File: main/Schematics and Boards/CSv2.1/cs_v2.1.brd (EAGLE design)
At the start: 38.1 x 47 mm, 78 parts, among them J101 J-JTAG-CORTEX-NEEDLE6-LEGS, J301 HIROSE-DF40_50-PIN_CONNECTORS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, J302 HIROSE-DF40_50-PIN_CONNECTORS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, Q1 DMG3415UFY4Q-7F, U1 NCP708MU330TAG, U101 ATSAMD51, U2 W25N01GVZEIG, U201 COULOMB-MAX17262, U202 MAX77827BEWC+T, U203 SENSOR-SI7006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

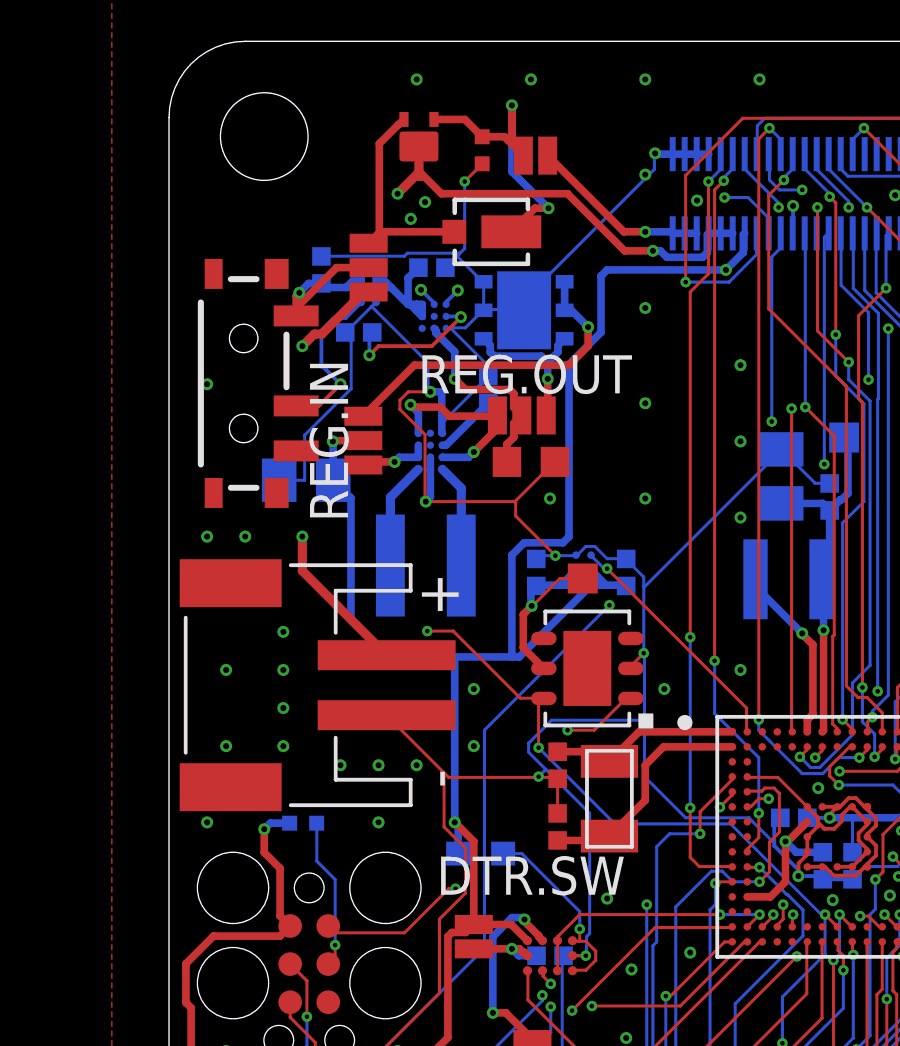
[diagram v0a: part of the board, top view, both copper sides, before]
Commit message: Rename 'base' to 'main' for consistency in terminology
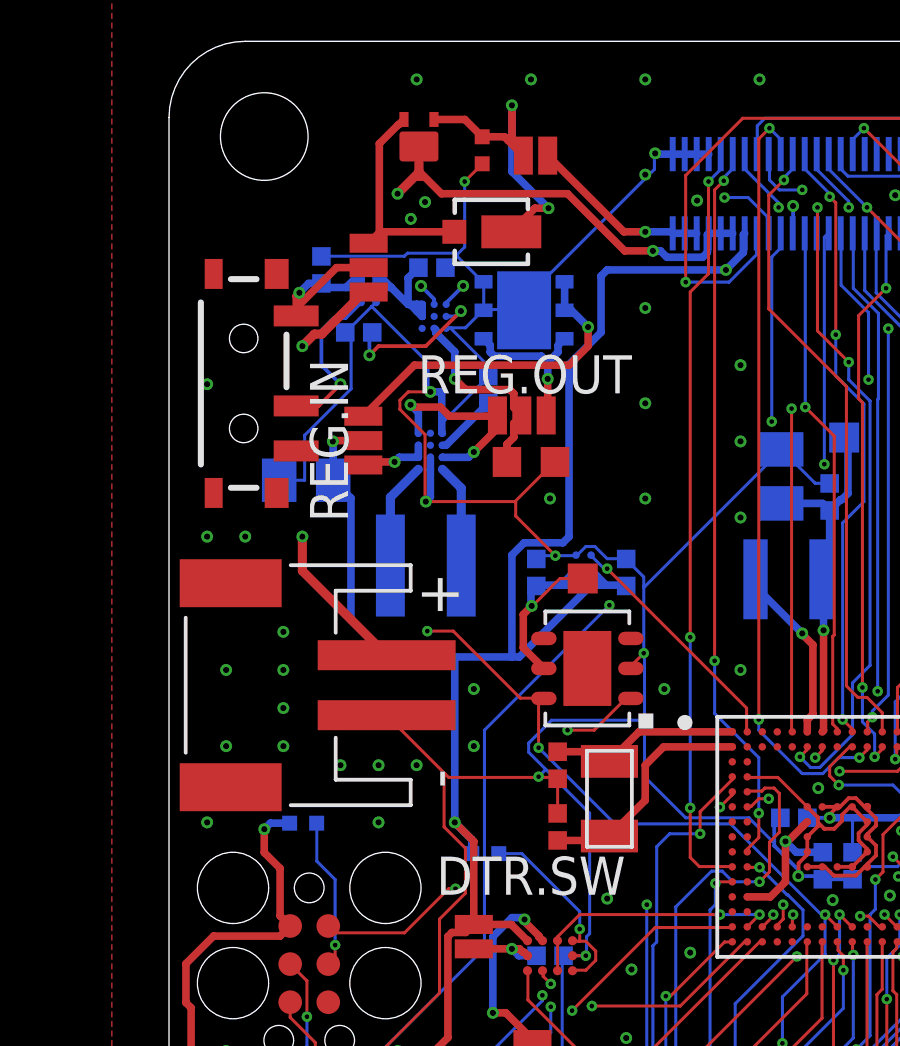
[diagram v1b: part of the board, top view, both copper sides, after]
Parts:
- R207: device Resistors:R0603 -> Resistors:R0402
- moved R207 0.15 mm to (10.5, 19.9)
